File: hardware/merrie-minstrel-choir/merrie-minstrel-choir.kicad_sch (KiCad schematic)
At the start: 23 parts, among them J1 USB_C, J2 Bell_Interface, J3 UART, U1 ESP32-S3-WROOM-1-N8, U2 AZ1117-3.3, U4 USBLC6-2SC6

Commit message: Choir board rev 2: fix EN pull-up, bottom-mount J2, shrink outline
- EN: R1 now pulls EN to +3.3V and C3 sits from EN to GND (rev 1 had
  R1 and C3 in series to GND with no pull-up).
- J2 card-edge socket moved to the bottom side in the same slot
  position. The upside-down socket maps card finger n to pin 25-n, so the
  schematic is re-pinned and every bell still reaches the same GPIO.
- Outline 33.5 x 53 mm (was 35 x 55), inside the rev 1 outline, with
  USB-C and the J2 mounting holes unmoved.
- Re-routed with Freerouting; GND trace cleanup guarded by DRC.
  Scripts and the DSN/SES job are in route/.

Co-Authored-By: Claude Opus 5.5 <noreply@anthropic.com>
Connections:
- net +3.3V: now also R1.1
- net Bell_1: now also J2.22; no longer J2.3
- net Bell_10: now also J2.5; no longer J2.20
- net Bell_11: now also J2.3; no longer J2.22
- net Bell_12: now also J2.1; no longer J2.24
- net Bell_2: now also J2.20; no longer J2.5
- net Bell_3: now also J2.18; no longer J2.7
- net Bell_4: now also J2.6; no longer J2.19
- net Bell_5: now also J2.4; no longer J2.21
- net Bell_6: now also J2.2; no longer J2.23
- net Bell_7: now also J2.21; no longer J2.4
- net Bell_8: now also J2.19; no longer J2.6
- net Bell_9: now also J2.17; no longer J2.8
- net EN: now also C3.1, R1.2; no longer R1.1
- net GND: now also J2.16; no longer J2.9
- net VCC: now also J2.15; no longer J2.10

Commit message: Choir rev 2: 0805 LEDs, 0603 resistors, J2 at the board edge
- D2/D3 to LED_0805, R1-R5 to R_0603 (hand-solder pads).
- J2 footprint without its mounting holes (card_edge_395024559212_noMH);
  the socket ears hang off the board, so the left edge moves in to
  0.5 mm outside the outer pin row. Board is now 26.8 x 53 mm.
- EN cap C3 moves next to C5; R1/C7/C8 sit in a row above J2.
- Re-routed and GND traces trimmed under DRC guard.

Co-Authored-By: Claude Opus 5.5 <noreply@anthropic.com>
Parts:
- D2, D3: footprint LED_SMD:LED_1206_3216Metric -> LED_SMD:LED_0805_2012Metric_Pad1.15x1.40mm_HandSolder
- J2: footprint footprints:card_edge_395024559212 -> footprints:card_edge_395024559212_noMH
- R1, R2, R3, R4, R5: footprint Resistor_SMD:R_0805_2012Metric_Pad1.20x1.40mm_HandSolder -> Resistor_SMD:R_0603_1608Metric_Pad0.98x0.95mm_HandSolder
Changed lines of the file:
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@@
 			)
 		)
-		(property "Footprint" "Resistor_SMD:R_0805_2012Metric_Pad1.20x1.40mm_HandSolder"
+		(property "Footprint" "Resistor_SMD:R_0603_1608Metric_Pad0.98x0.95mm_HandSolder"
 			(at 32.766 117.094 90)
 			(hide yes)
@@
 			)
 		)
-		(property "Footprint" "Resistor_SMD:R_0805_2012Metric_Pad1.20x1.40mm_HandSolder"
+		(property "Footprint" "Resistor_SMD:R_0603_1608Metric_Pad0.98x0.95mm_HandSolder"
 			(at 178.054 122.174 90)
 			(hide yes)
@@
 			)
 		)
-		(property "Footprint" "Resistor_SMD:R_0805_2012Metric_Pad1.20x1.40mm_HandSolder"
+		(property "Footprint" "Resistor_SMD:R_0603_1608Metric_Pad0.98x0.95mm_HandSolder"
 			(at 90.424 23.114 90)
 			(hide yes)
@@
 			)
 		)
-		(property "Footprint" "LED_SMD:LED_1206_3216Metric"
+		(property "Footprint" "LED_SMD:LED_0805_2012Metric_Pad1.15x1.40mm_HandSolder"
 			(at 274.32 45.72 0)
 			(hide yes)
@@
 			)
 		)
-		(property "Footprint" "Resistor_SMD:R_0805_2012Metric_Pad1.20x1.40mm_HandSolder"
+		(property "Footprint" "Resistor_SMD:R_0603_1608Metric_Pad0.98x0.95mm_HandSolder"
 			(at 275.336 35.814 90)
 			(hide yes)
@@
 			)
 		)
-		(property "Footprint" "LED_SMD:LED_1206_3216Metric"
+		(property "Footprint" "LED_SMD:LED_0805_2012Metric_Pad1.15x1.40mm_HandSolder"
 			(at 189.23 123.19 0)
 			(hide yes)
@@
 			)
 		)
-		(property "Footprint" "Resistor_SMD:R_0805_2012Metric_Pad1.20x1.40mm_HandSolder"
+		(property "Footprint" "Resistor_SMD:R_0603_1608Metric_Pad0.98x0.95mm_HandSolder"
 			(at 90.424 28.194 90)
 			(hide yes)
@@
 			)
 		)
-		(property "Footprint" "footprints:card_edge_395024559212"
+		(property "Footprint" "footprints:card_edge_395024559212_noMH"
 			(at 236.22 183.82 0)
 			(hide yes)

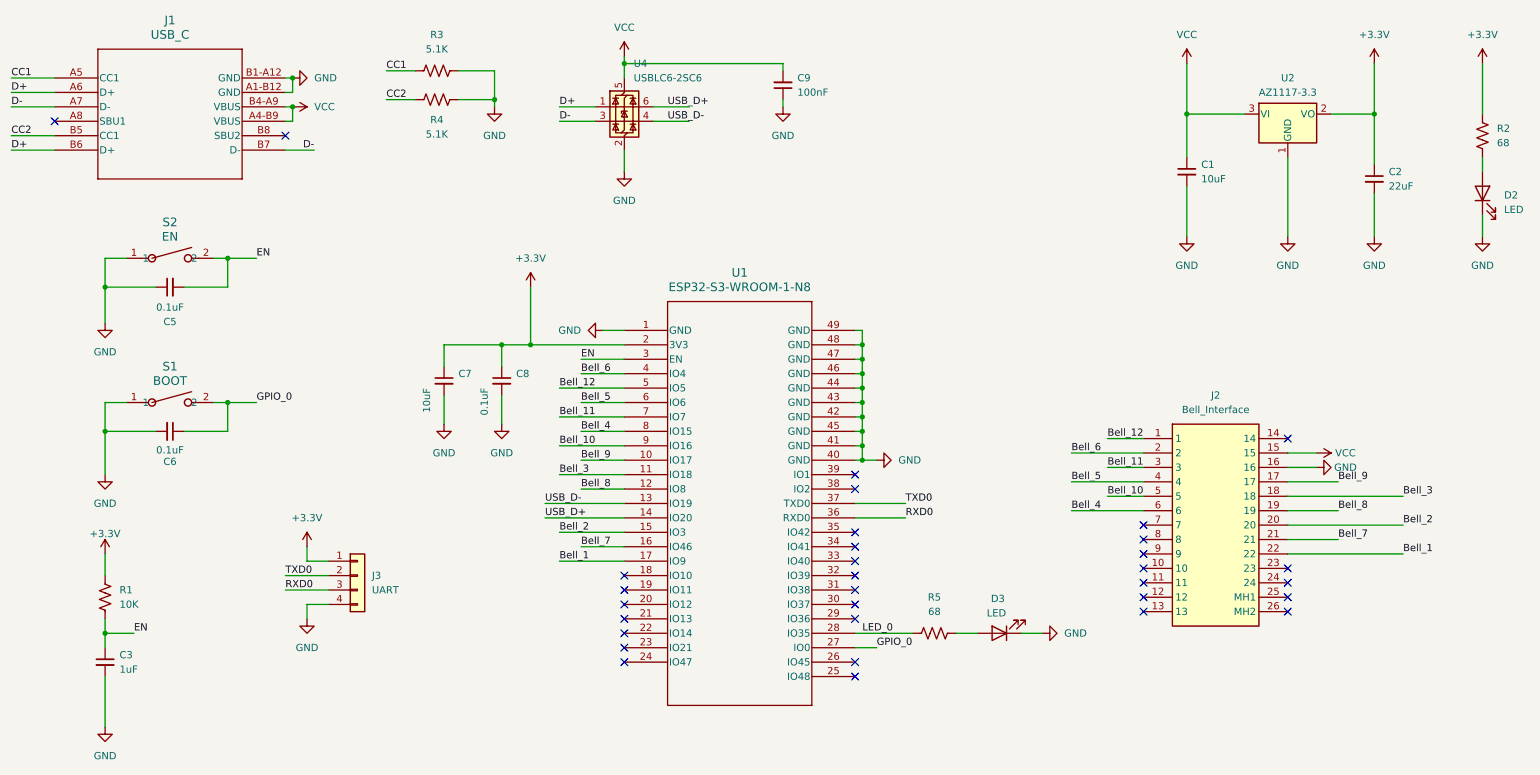
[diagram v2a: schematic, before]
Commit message: Choir rev 2: R/C to the back, shrink to 26.8 x 37 mm, schematic fixes
Layout:
- Every resistor and capacitor moves to the back, behind the part it serves.
- The board shrinks to 26.8 x 37 mm. J1 moves up 10 mm, so the enclosure's
  USB-C opening has to move too.
- The J1/U4/C9 corner is hand-routed and locked; the rest is re-routed with
  Freerouting, and the redundant GND traces are removed.
- Silkscreen references are re-placed at the 0.8 mm minimum.
- New scripts: route/v3_layout.py, usb_v3.py, silk_v3.py.

Schematic:
- Adds R6, a 10k pull-up on GPIO0. BOOT stays, for serial flashing and as a
  user button.
- Removes the button caps C5 and C6.
- R2/R5 are now 1.5k, so the LEDs glow dimly.
- S1/S2 move to the TS-1088 footprint.
- ERC is clean: PWR_FLAGs added and pin types fixed in the vendor libraries.
- Adds a project-local sym-lib-table and fp-lib-table and a footprints.pretty
  library, plus a rebuilt symbol for the EDAC 395-024-559-212 socket.

Co-Authored-By: Claude Opus 5.5 <noreply@anthropic.com>
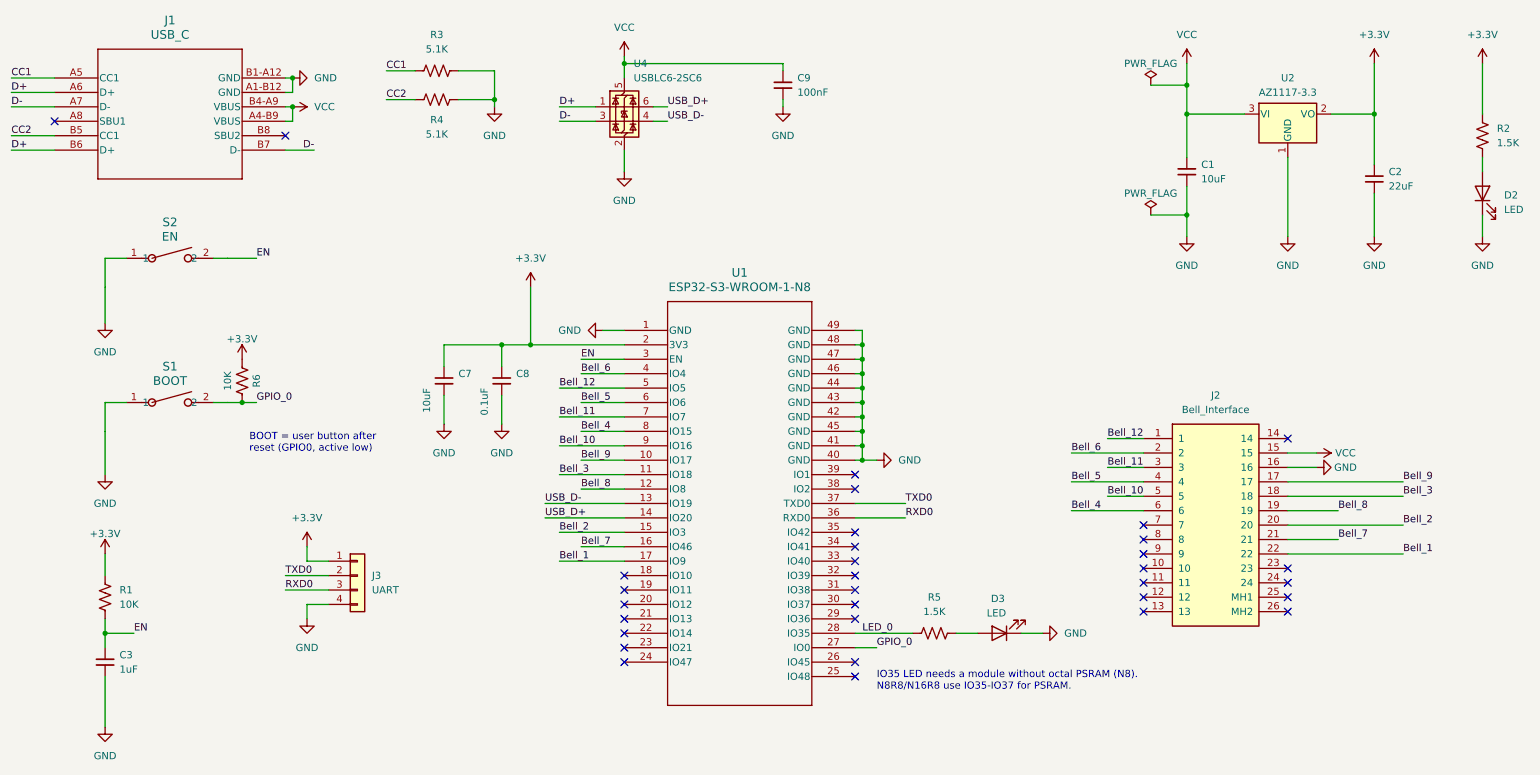
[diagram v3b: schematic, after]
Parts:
- removed C5, C6: 0.1uF, Capacitor_SMD:C_0805_2012Metric_Pad1.18x1.45mm_HandSolder, symbol Device:C_Small
- added R6: 10K, Resistor_SMD:R_0603_1608Metric_Pad0.98x0.95mm_HandSolder, symbol Device:R_US
- R2, R5: value 68 -> 1.5K
- S1, S2: footprint Button_Switch_SMD:SW_SPST_CK_RS282G05A3 -> Button_Switch_SMD:SW_SPST_TS-1088-xR020; Manufacturer_Name (none) -> XUNPU; Manufacturer_Part_Number (none) -> TS-1088-AR02016
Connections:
- net +3.3V: now also R6.1
- net GPIO_0: now also R6.2
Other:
- note added: "BOOT = user button after reset (GPIO0, active low)"
- note added: "IO35 LED needs a module without octal PSRAM (N8). N8R8/N16R8 use IO35-IO37 for PSRAM."
